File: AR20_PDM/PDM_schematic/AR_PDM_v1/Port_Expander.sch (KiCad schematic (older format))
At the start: 15 parts, among them U42 N-MOS, U43 N-MOS, U9 TCA6424ARGJR

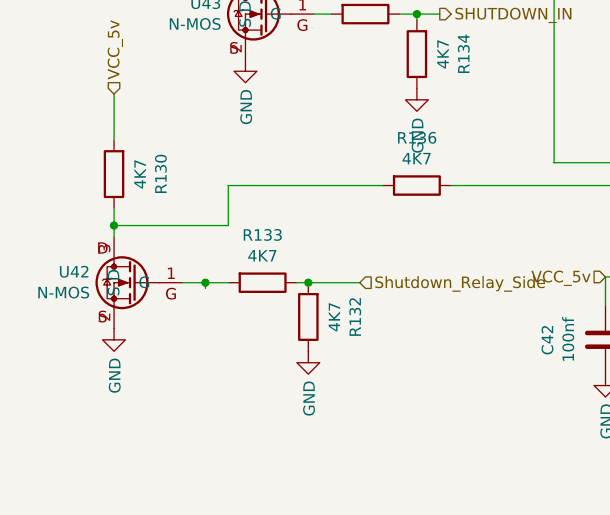
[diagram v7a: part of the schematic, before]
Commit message: shematics adjustments, and fixing values and names
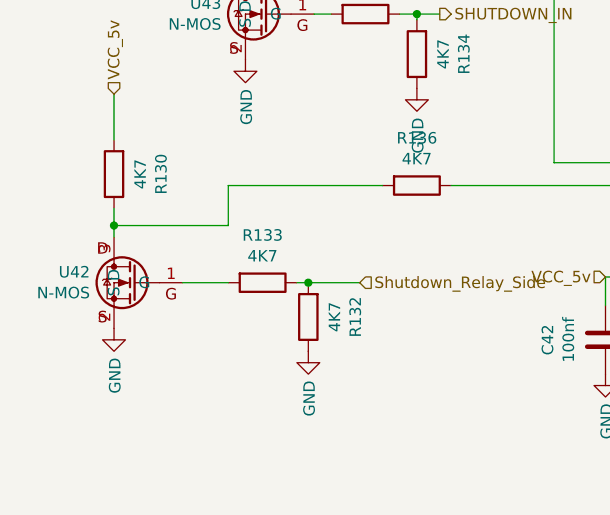
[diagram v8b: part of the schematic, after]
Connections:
- wire segments 32 -> 30
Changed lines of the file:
@@
 	1    0    0    -1
 $EndComp
-Wire Wire Line
-	2400 4375 2500 4375
-Wire Wire Line
-	2500 4375 2500 4400
-Wire Wire Line
-	2500 4375 2600 4375
-Connection ~ 2500 4375
 Text HLabel 3525 3200 2    50   Output ~ 0
 SHUTDOWN_IN
@@
 	2950 4375 3175 4375
 Connection ~ 2950 4375
+Wire Wire Line
+	2400 4375 2600 4375
 $EndSCHEMATC
